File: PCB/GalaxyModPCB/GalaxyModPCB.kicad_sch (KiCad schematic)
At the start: 58 parts, among them J1 Power Header, J2 Boot mode, J3 LED RGBW Connector, J4 USB to UART, J5 Motor Connector, J6 Projector Connector, Q1 IRLML0030, Q2 IRLML0030, Q3 IRLML0030, Q4 IRLML0030, Q5 IRLML0030, Q6 IRLML0030, SW1 Motor, SW2 Brightness, SW3 Colour, SW4 On/Off, U1 AMS1117-3.3, U2 ESP32-WROOM-32

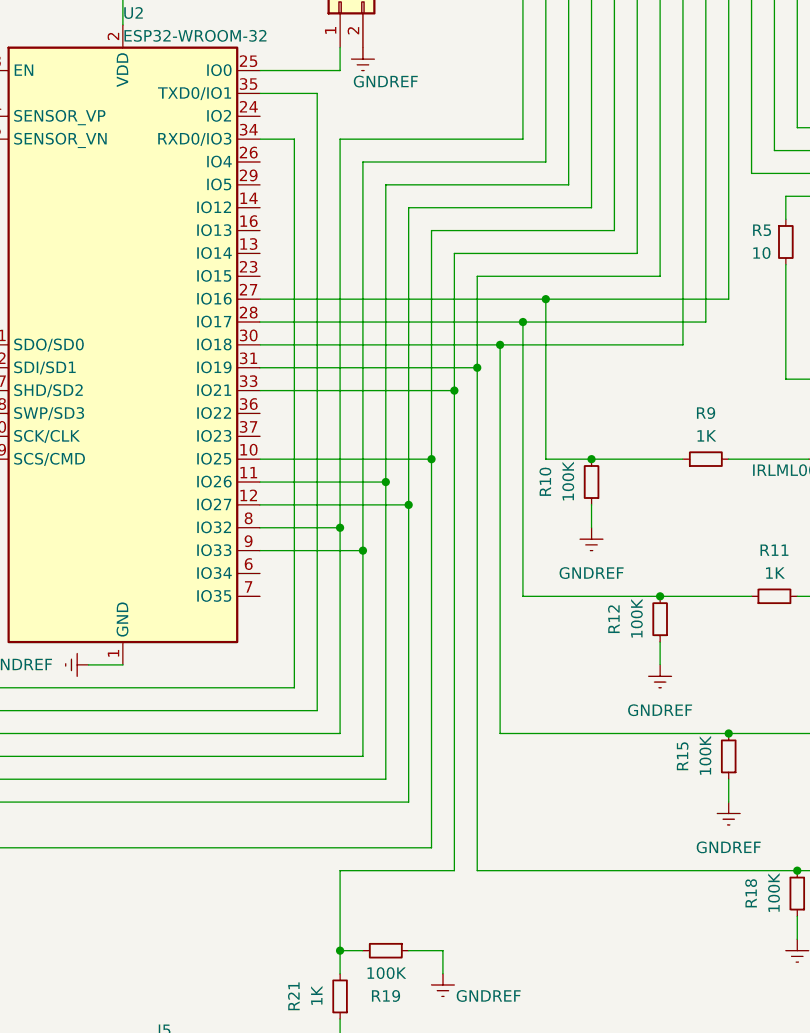
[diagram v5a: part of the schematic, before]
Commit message: Rearranged and wired inputs
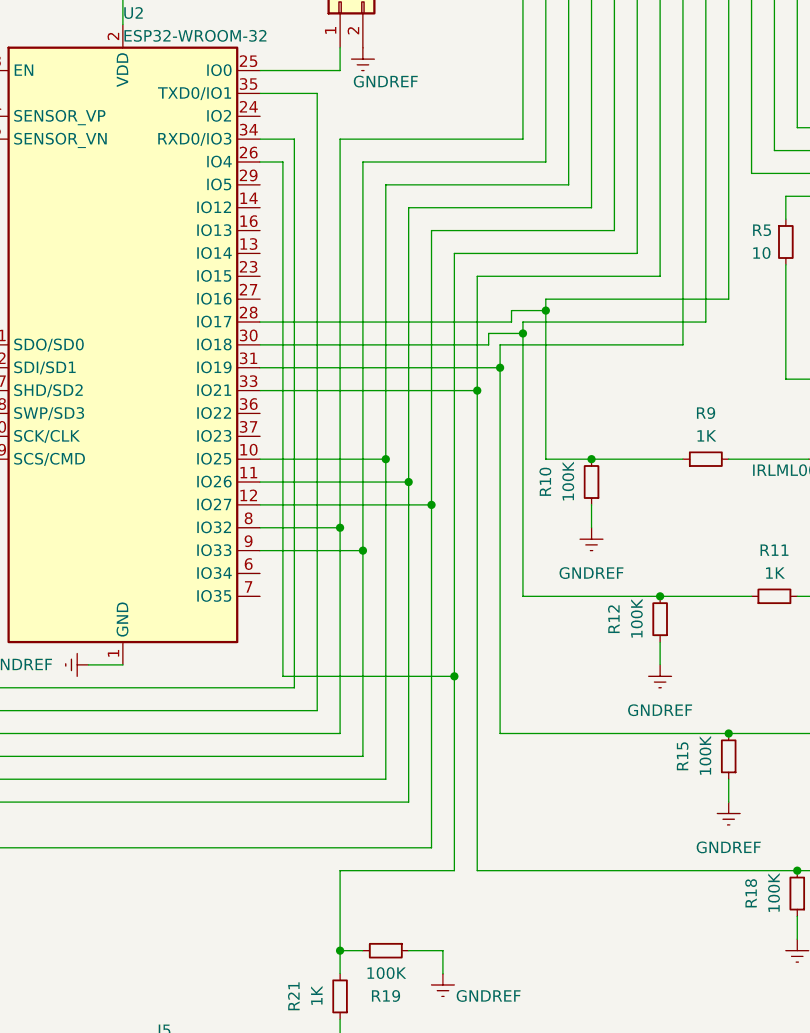
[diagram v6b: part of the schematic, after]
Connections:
- net at R14.1, R15.2: now also U2.31 (IO19); no longer U2.30 (IO18)
- net at R22.2, R23.2: now also U2.12 (IO27); no longer U2.10 (IO25)
- net at C7.1, R20.2, SW3.1: now also U2.10 (IO25); no longer U2.11 (IO26)
- net at C8.1, R24.2, SW4.1: now also U2.11 (IO26); no longer U2.12 (IO27)
- net at U2.26 (IO4): now also R19.2, R21.2
- net at R10.2, R9.1: now also U2.28 (IO17); no longer U2.27 (IO16)
- net at R11.1, R12.2: now also U2.30 (IO18); no longer U2.28 (IO17)
- net at R17.1, R18.2: now also U2.33 (IO21); no longer U2.31 (IO19)

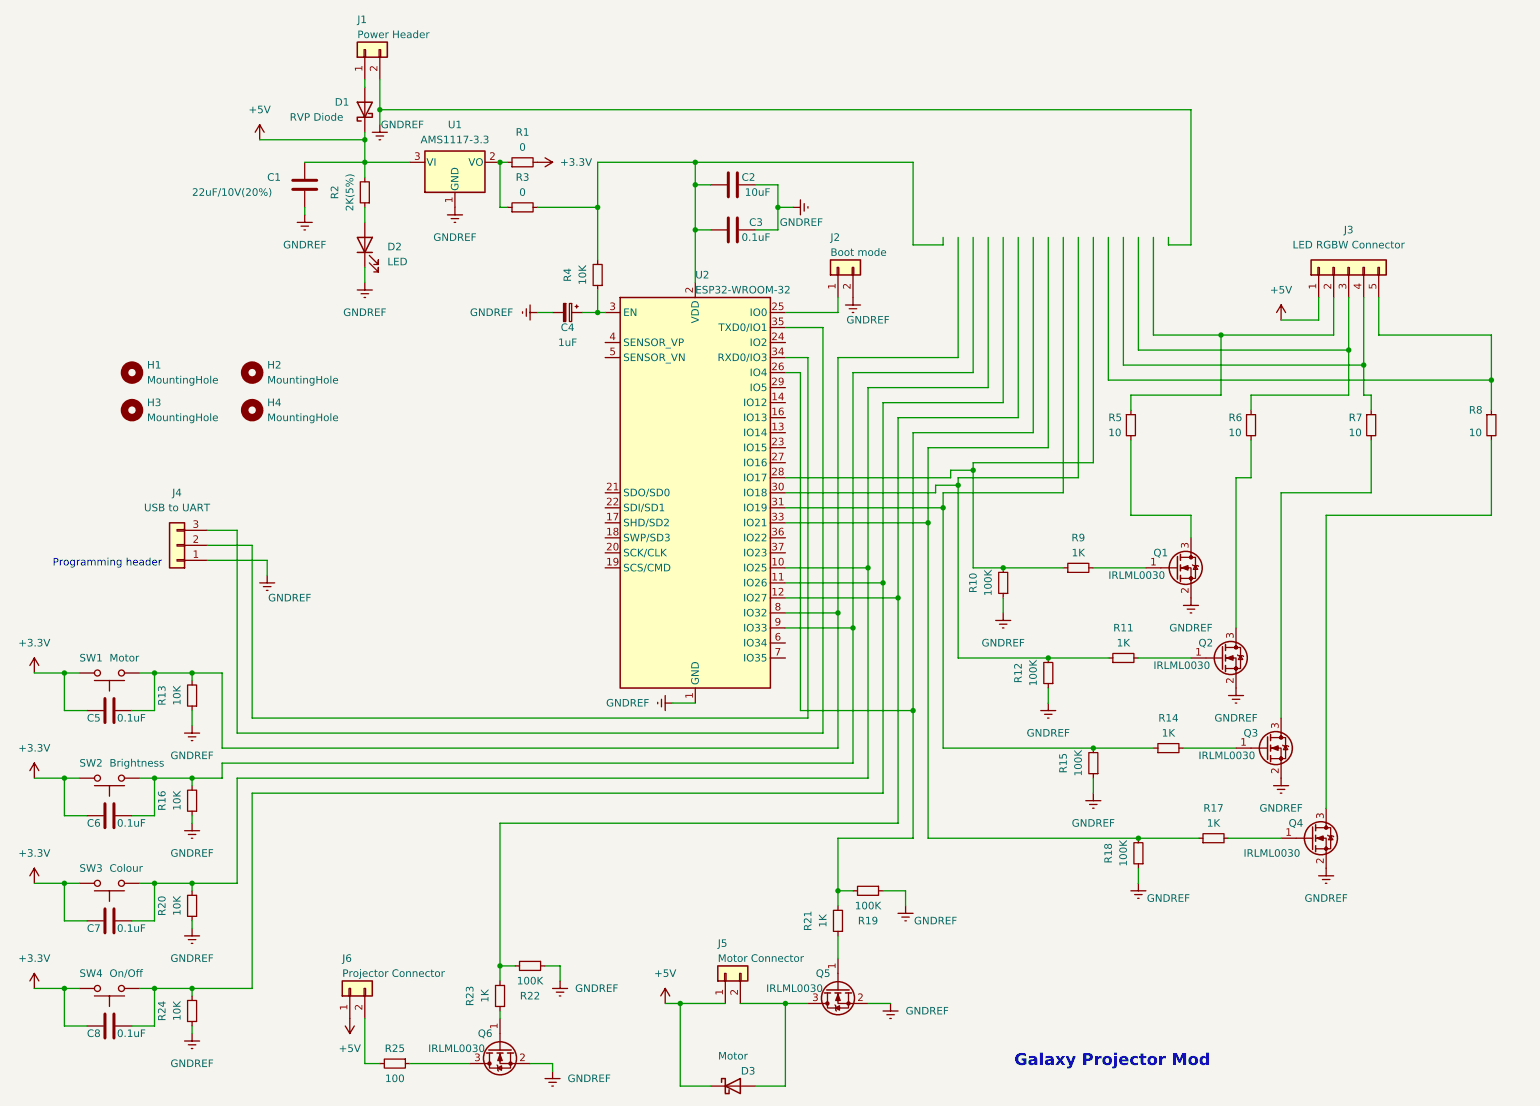
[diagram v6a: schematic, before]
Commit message: Re-wired switches
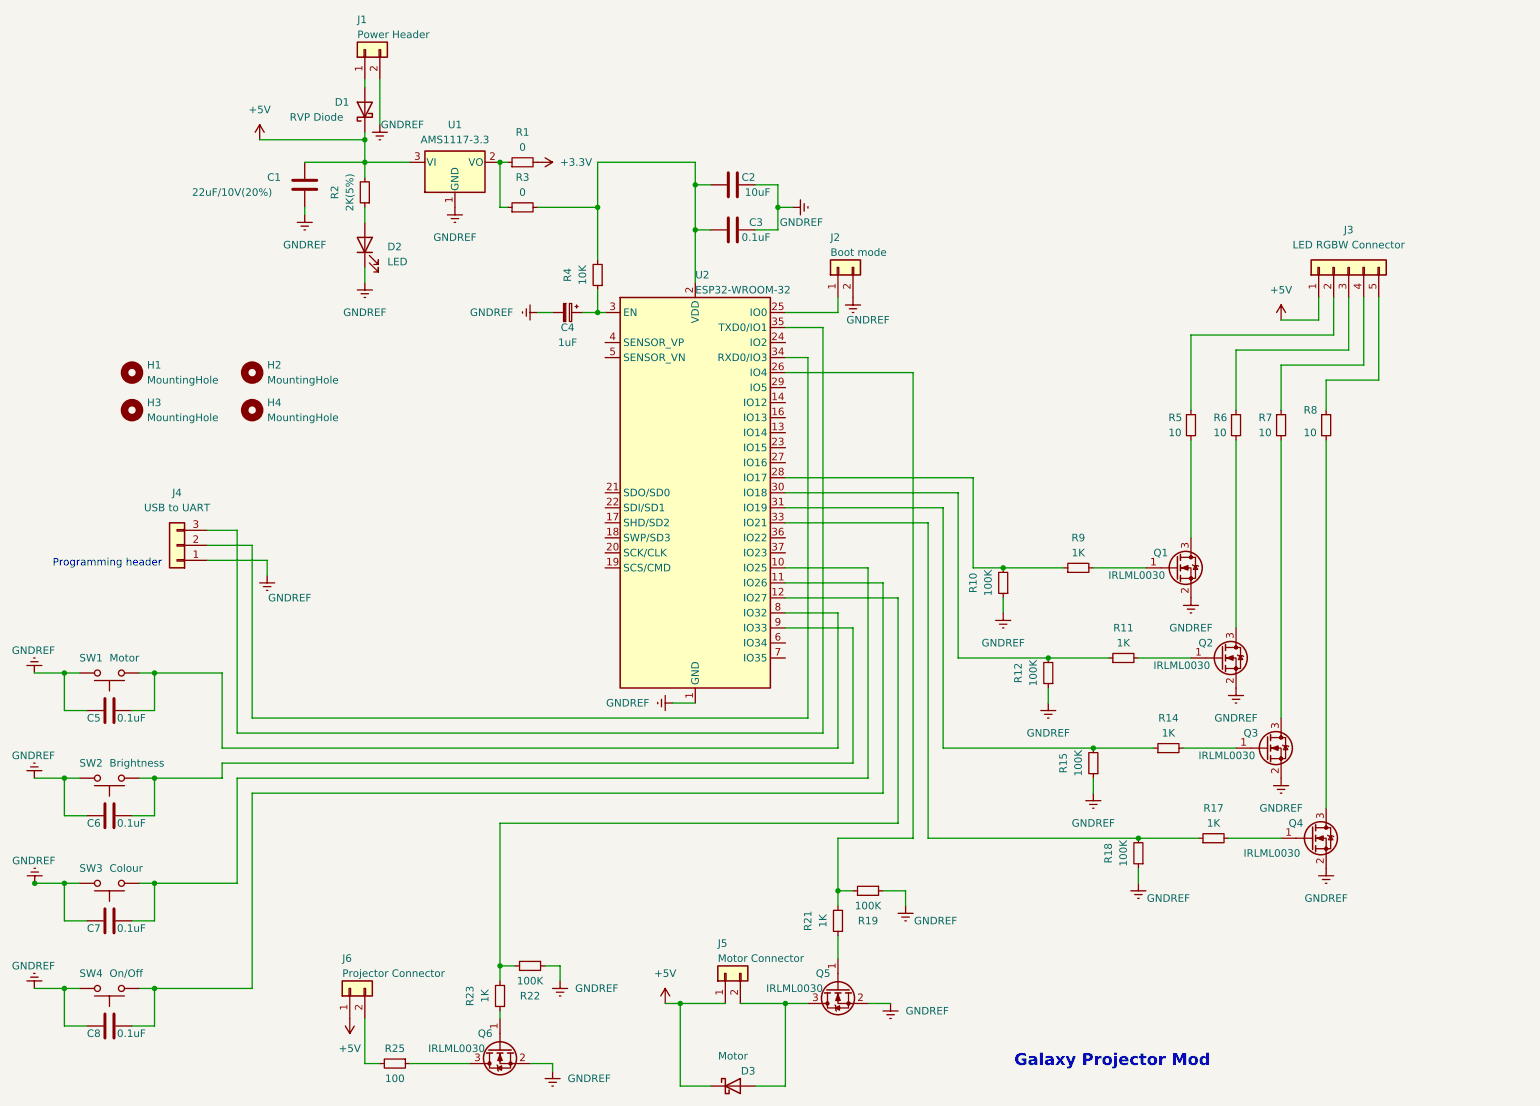
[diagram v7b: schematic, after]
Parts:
- removed R13, R16, R20, R24: 10K, Resistor_SMD:R_0805_2012Metric_Pad1.20x1.40mm_HandSolder, symbol Device:R_Small
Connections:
- net +3.3V: no longer C5.2, C6.2, C7.2, C8.2, SW1.2, SW2.2, SW3.2, SW4.2
- net GNDREF: now also C5.2, C6.2, C7.2, C8.2, SW1.2, SW2.2, SW3.2, SW4.2
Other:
- moved on the sheet: R5, R6, R7, R8

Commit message: Added documentation
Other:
- note added: "1 of 1"
- note added: "1.0"
- note added: "August 2023"
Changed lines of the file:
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@@
     (stroke (width 0) (type default) (color 0 0 0 0))
+  )
+  (text "1.0" (at 267.97 194.31 0)
+    (effects (font (size 1.5 1.5)) (justify left bottom))
   )
   (text "Galaxy Projector Mod" (at 186.0228 191.2366 0)
     (effects (font (size 2 2) (thickness 0.4) bold) (justify left bottom))
   )
+  (text "1 of 1" (at 189.23 184.15 0)
+    (effects (font (size 1.5 1.5)) (justify left bottom))
+  )
+  (text "August 2023" (at 207.01 194.31 0)
+    (effects (font (size 1.5 1.5)) (justify left bottom))
+  )
   (text "Programming header" (at 41.91 106.68 180)
